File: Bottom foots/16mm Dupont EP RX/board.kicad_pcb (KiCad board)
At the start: 2 copper layers, 24 x 35.1 mm, 22 parts, among them J1 Conn_01x06, J10 Conn_01x01, J11 Conn_01x03, J12 Conn_01x01, J13 Conn_01x01, J2 Conn_01x03, J3 Conn_01x03, J4 Conn_01x03, J5 Conn_01x03, J6 Conn_01x01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

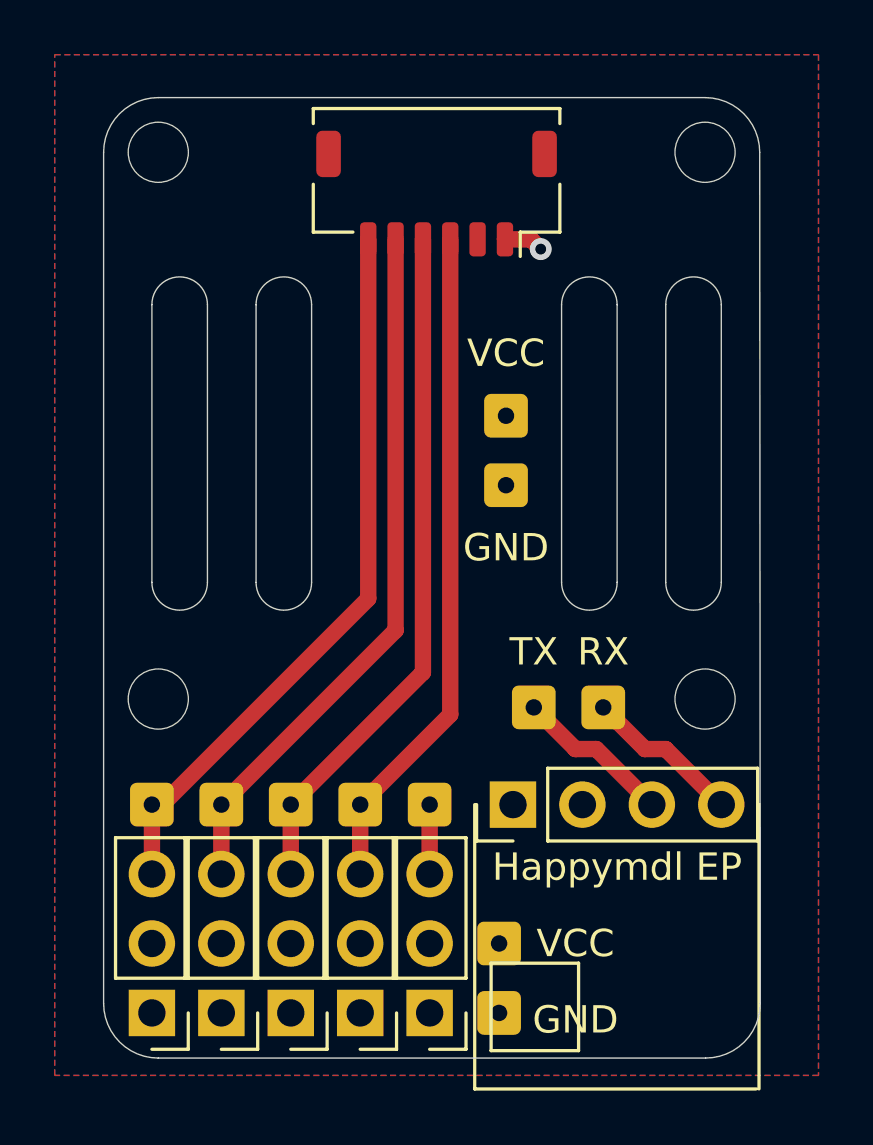
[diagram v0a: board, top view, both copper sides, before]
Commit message: Space out the VCC path a bit.
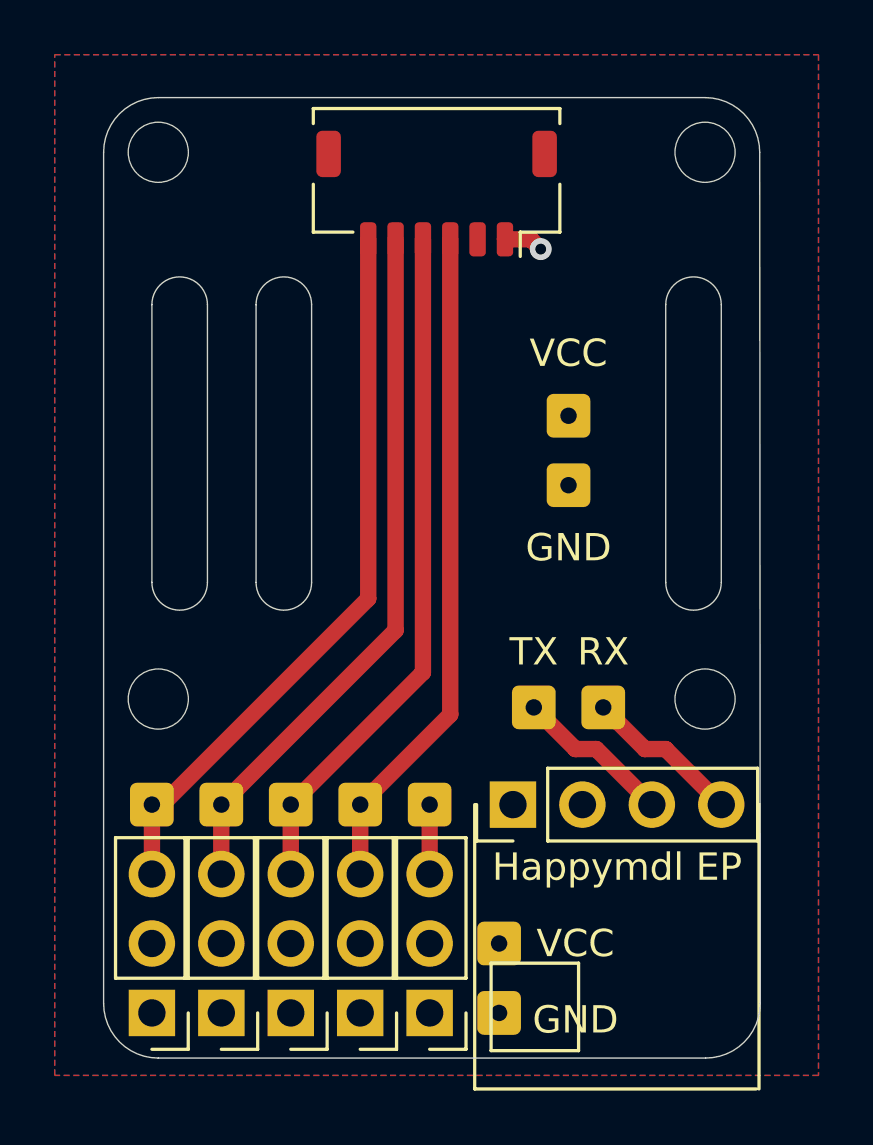
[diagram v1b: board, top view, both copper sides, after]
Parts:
- moved J10 2.29 mm to (117.6, 112.0)
- moved J6 2.29 mm to (117.6, 114.6)
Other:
- outline, holes or cut-outs redrawn
